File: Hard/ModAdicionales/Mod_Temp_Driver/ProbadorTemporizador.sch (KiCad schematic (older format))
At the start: 10 parts

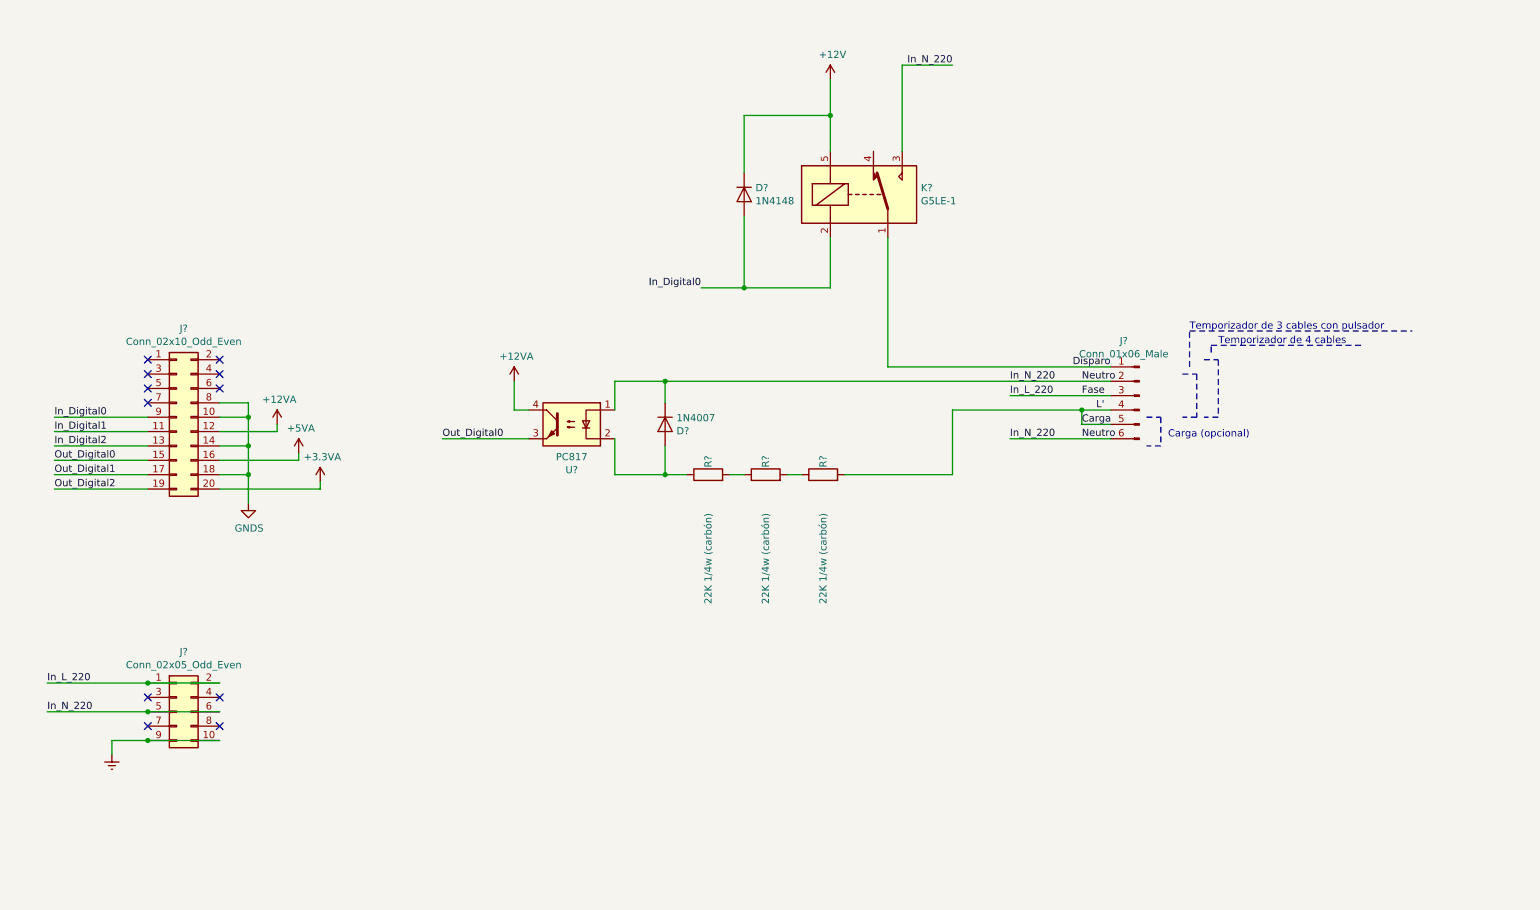
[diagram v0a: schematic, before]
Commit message: Primera correccion en modulos Adicionales y cambio de etapa de salida en modulo principal
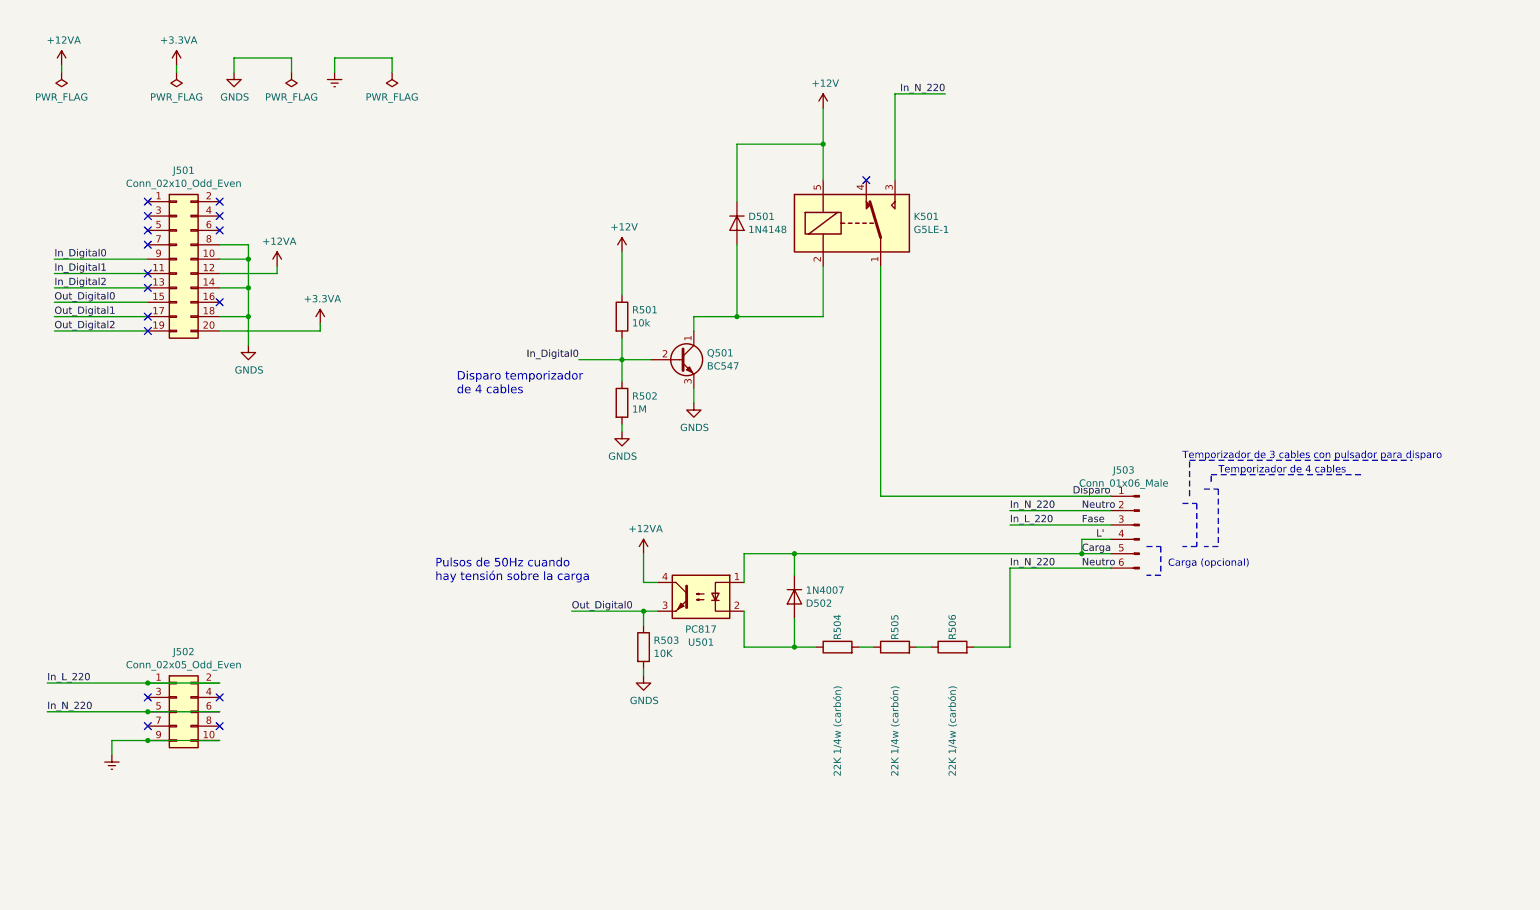
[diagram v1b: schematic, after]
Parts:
- added Q501: BC547, Package_TO_SOT_THT:TO-92_Inline, symbol Transistor_BJT:BC547
- added R501: 10k, Resistor_SMD:R_0805_2012Metric_Pad1.15x1.40mm_HandSolder, symbol Device:R
- added R502: 1M, Resistor_SMD:R_0805_2012Metric_Pad1.15x1.40mm_HandSolder, symbol Device:R
- added R503: 10K, Resistor_SMD:R_0805_2012Metric_Pad1.15x1.40mm_HandSolder, symbol Device:R
- gave numbers to parts that had none: 10
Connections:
- net +12V: now also R501.1
- net Carga: now also D502.1 (K), U501.1; no longer R506.2
- net GNDS: now also Q501.3 (E), R502.2, R503.2
- net In_Digital0: now also Q501.2 (B), R501.2, R502.1; no longer D501.2 (A), K501.2
- net In_N_220: now also R506.2; no longer D502.1 (K), U501.1
- net Out_Digital0: now also R503.1
- net +5VA: no longer names the net of J501.16 (Pin_16)
- new net: D501.2 (A), K501.2, Q501.1 (C)
- no-connect marks 11 -> 17
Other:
- note added: "Disparo temporizador\nde 4 cables"
- note added: "Pulsos de 50Hz cuando \nhay tensión sobre la carga"
- note added: "Temporizador de 3 cables con pulsador para disparo"
- note removed: "Temporizador de 3 cables con pulsador"
- moved on the sheet: D501, D502, J501, J503, K501, R504, R505, R506, U501

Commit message: Asignacion de footprints Modulos adicionales
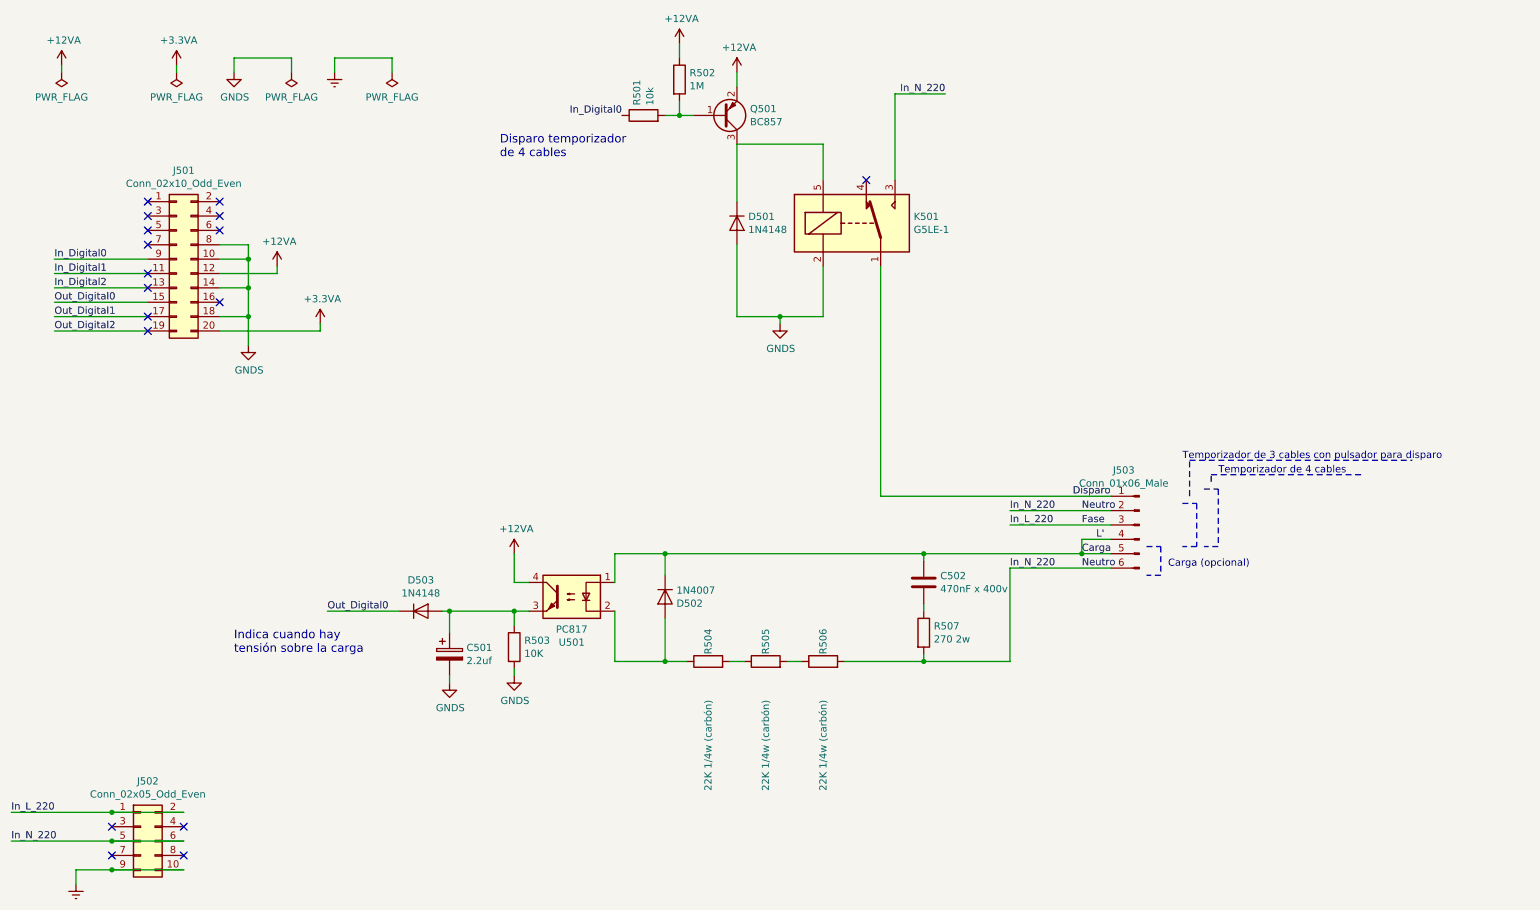
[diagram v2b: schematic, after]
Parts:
- removed Q501: BC547, Package_TO_SOT_THT:TO-92_Inline, symbol Transistor_BJT:BC547
- added C501: 2.2uf, Capacitor_THT:CP_Radial_D5.0mm_P2.00mm, symbol Device:CP
- added C502: 470nF x 400v, Capacitor_THT:C_Rect_L16.5mm_W8.7mm_P15.00mm_MKT, symbol Device:C
- added D503: 1N4148, Diode_THT:D_DO-35_SOD27_P7.62mm_Horizontal, symbol Diode:1N4148
- added Q501: BC857, Package_TO_SOT_SMD:SOT-23, symbol Transistor_BJT:BC857
- added R507: 270 2w, Resistor_THT:R_Axial_DIN0516_L15.5mm_D5.0mm_P20.32mm_Horizontal, symbol Device:R
- J501: footprint (none) -> Connector_PinHeader_2.54mm:PinHeader_2x10_P2.54mm_Horizontal
- J502: footprint (none) -> Connector_PinHeader_2.54mm:PinHeader_2x05_P2.54mm_Horizontal
- J503: footprint (none) -> TerminalBlock_Altech:Altech_AK300_1x06_P5.00mm_45-Degree
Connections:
- net +12VA: now also R502.1, Q501.2 (E)
- net Carga: now also C502.1
- net GNDS: now also D501.2 (A), K501.2, C501.2; no longer R502.2
- net In_Digital0: now also R501.1; no longer R501.2, R502.1
- net In_N_220: now also R507.2
- net Out_Digital0: now also D503.1 (K); no longer R503.1, U501.3
- net +12V: no longer names the net of D501.1 (K), K501.5
- net +12V: now also Q501.3 (C); no longer R501.1
- new net: C501.1, D503.2 (A), R503.1, U501.3
- new net: Q501.1 (B), R501.2, R502.2
- new net: C502.2, R507.1
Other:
- note added: "Indica cuando hay\ntensión sobre la carga"
- note removed: "Pulsos de 50Hz cuando \nhay tensión sobre la carga"
- moved on the sheet: D502, J502, R503, R504, R505, R506, U501

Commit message: Inicio placement de componentes en Modulos Adicionales
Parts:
- added H501, H502, H503, H504: MountingHole, MountingHole:MountingHole_3.2mm_M3, symbol Mechanical:MountingHole
- D503: footprint Diode_THT:D_DO-35_SOD27_P7.62mm_Horizontal -> Diode_SMD:D_MiniMELF
- J503: footprint TerminalBlock_Altech:Altech_AK300_1x06_P5.00mm_45-Degree -> Conectores:TerminalBlock_bornier-6_P5.00mm
- R504, R505, R506: footprint Resistor_THT:R_Axial_DIN0309_L9.0mm_D3.2mm_P12.70mm_Horizontal -> Resistor_THT:R_Axial_DIN0207_L6.3mm_D2.5mm_P7.62mm_Horizontal
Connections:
- net Carga: now also R506.2; no longer D502.1 (K), U501.1
- net In_N_220: now also D502.2 (A), U501.2; no longer R506.2
- new net: D502.1 (K), R504.1, U501.1
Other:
- moved on the sheet: R504, R505, R506
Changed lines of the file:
@@
 EESchema Schematic File Version 4
-LIBS:Mod_Temp_Driver-cache
 EELAYER 30 0
 EELAYER END
@@
 F 0 "J503" H 8958 4631 50  0000 C CNN
 F 1 "Conn_01x06_Male" H 8958 4540 50  0000 C CNN
-F 2 "TerminalBlock_Altech:Altech_AK300_1x06_P5.00mm_45-Degree" H 8850 4250 50  0001 C CNN
+F 2 "Conectores:TerminalBlock_bornier-6_P5.00mm" H 8850 4250 50  0001 C CNN
 F 3 "~" H 8850 4250 50  0001 C CNN
 	1    8850 4250
@@
 L Device:R R?
 U 1 1 5F49E33D
-P 6650 5200
+P 6650 4450
 AR Path="/5ED5374F/5F49E33D" Ref="R?"  Part="1"
 AR Path="/5ED5374F/5F0ECABF/5F49E33D" Ref="R?"  Part="1"
 AR Path="/5ED538D0/5F49E33D" Ref="R506"  Part="1"
-F 0 "R506" H 6700 5200 50  0000 L CNN
-F 1 "22K 1/4w (carbón)" H 5750 5200 50  0000 L CNN
-F 2 "Resistor_THT:R_Axial_DIN0309_L9.0mm_D3.2mm_P12.70mm_Horizontal" V 6580 5200 50  0001 C CNN
-F 3 "~" H 6650 5200 50  0001 C CNN
-	1    6650 5200
+F 0 "R506" H 6700 4450 50  0000 L CNN
+F 1 "22K 1/4w (carbón)" H 5750 4450 50  0000 L CNN
+F 2 "Resistor_THT:R_Axial_DIN0207_L6.3mm_D2.5mm_P7.62mm_Horizontal" V 6580 4450 50  0001 C CNN
+F 3 "~" H 6650 4450 50  0001 C CNN
+	1    6650 4450
 	0    -1   -1   0
 $EndComp
@@
 L Device:R R?
 U 1 1 5F49E343
-P 6250 5200
+P 6250 4450
 AR Path="/5ED5374F/5F49E343" Ref="R?"  Part="1"
 AR Path="/5ED5374F/5F0ECABF/5F49E343" Ref="R?"  Part="1"
 AR Path="/5ED538D0/5F49E343" Ref="R505"  Part="1"
-F 0 "R505" H 6300 5200 50  0000 L CNN
-F 1 "22K 1/4w (carbón)" H 5350 5200 50  0000 L CNN
-F 2 "Resistor_THT:R_Axial_DIN0309_L9.0mm_D3.2mm_P12.70mm_Horizontal" V 6180 5200 50  0001 C CNN
-F 3 "~" H 6250 5200 50  0001 C CNN
-	1    6250 5200
+F 0 "R505" H 6300 4450 50  0000 L CNN
+F 1 "22K 1/4w (carbón)" H 5350 4450 50  0000 L CNN
+F 2 "Resistor_THT:R_Axial_DIN0207_L6.3mm_D2.5mm_P7.62mm_Horizontal" V 6180 4450 50  0001 C CNN
+F 3 "~" H 6250 4450 50  0001 C CNN
+	1    6250 4450
 	0    -1   -1   0
 $EndComp
@@
 L Device:R R?
 U 1 1 5F49E349
-P 5850 5200
+P 5850 4450
 AR Path="/5ED5374F/5F49E349" Ref="R?"  Part="1"
 AR Path="/5ED5374F/5F0ECABF/5F49E349" Ref="R?"  Part="1"
 AR Path="/5ED538D0/5F49E349" Ref="R504"  Part="1"
-F 0 "R504" H 5900 5200 50  0000 L CNN
-F 1 "22K 1/4w (carbón)" H 4950 5200 50  0000 L CNN
-F 2 "Resistor_THT:R_Axial_DIN0309_L9.0mm_D3.2mm_P12.70mm_Horizontal" V 5780 5200 50  0001 C CNN
-F 3 "~" H 5850 5200 50  0001 C CNN
-	1    5850 5200
+F 0 "R504" H 5900 4450 50  0000 L CNN
+F 1 "22K 1/4w (carbón)" H 4950 4450 50  0000 L CNN
+F 2 "Resistor_THT:R_Axial_DIN0207_L6.3mm_D2.5mm_P7.62mm_Horizontal" V 5780 4450 50  0001 C CNN
+F 3 "~" H 5850 4450 50  0001 C CNN
+	1    5850 4450
 	0    -1   -1   0
 $EndComp
 Wire Wire Line
-	6000 5200 6100 5200
-Wire Wire Line
-	6400 5200 6500 5200
+	6000 4450 6100 4450
+Wire Wire Line
+	6400 4450 6500 4450
 Wire Wire Line
 	8650 4350 8450 4350
@@
 	8650 4150 7950 4150
 Wire Wire Line
-	5550 4450 7350 4450
-Connection ~ 5550 4450
+	5550 5200 7350 5200
 Wire Wire Line
 	8650 4550 7950 4550
@@
 F 0 "D503" H 3850 5066 50  0000 C CNN
 F 1 "1N4148" H 3850 4975 50  0000 C CNN
-F 2 "Diode_THT:D_DO-35_SOD27_P7.62mm_Horizontal" H 3850 4675 50  0001 C CNN
+F 2 "Diode_SMD:D_MiniMELF" H 3850 4675 50  0001 C CNN
 F 3 "https://assets.nexperia.com/documents/data-sheet/1N4148_1N4448.pdf" H 3850 4850 50  0001 C CNN
 	1    3850 4850
@@
 Wire Wire Line
 	7350 4500 7350 4450
-Connection ~ 7350 4450
 Wire Wire Line
 	7350 4450 8450 4450
@@
 	5200 4850 5200 5200
 Wire Wire Line
-	6800 5200 7350 5200
+	6800 4450 7350 4450
+Wire Wire Line
+	5550 4900 5550 5200
+Wire Wire Line
+	5550 4450 5700 4450
+$Comp
+L Mechanical:MountingHole H?
+U 1 1 5ED84BD0
+P 9300 1150
+AR Path="/5ED5374F/5ED84BD0" Ref="H?"  Part="1"
+AR Path="/5ED538D0/5ED84BD0" Ref="H501"  Part="1"
+F 0 "H501" H 9400 1196 50  0000 L CNN
+F 1 "MountingHole" H 9400 1105 50  0000 L CNN
+F 2 "MountingHole:MountingHole_3.2mm_M3" H 9300 1150 50  0001 C CNN
+F 3 "~" H 9300 1150 50  0001 C CNN
+	1    9300 1150
+	1    0    0    -1
+$EndComp
+$Comp
+L Mechanical:MountingHole H?
+U 1 1 5ED84BD6
+P 10300 1150
+AR Path="/5ED5374F/5ED84BD6" Ref="H?"  Part="1"
+AR Path="/5ED538D0/5ED84BD6" Ref="H503"  Part="1"
+F 0 "H503" H 10400 1196 50  0000 L CNN
+F 1 "MountingHole" H 10400 1105 50  0000 L CNN
+F 2 "MountingHole:MountingHole_3.2mm_M3" H 10300 1150 50  0001 C CNN
+F 3 "~" H 10300 1150 50  0001 C CNN
+	1    10300 1150
+	1    0    0    -1
+$EndComp
+$Comp
+L Mechanical:MountingHole H?
+U 1 1 5ED84BDC
+P 9300 1550
+AR Path="/5ED5374F/5ED84BDC" Ref="H?"  Part="1"
+AR Path="/5ED538D0/5ED84BDC" Ref="H502"  Part="1"
+F 0 "H502" H 9400 1596 50  0000 L CNN
+F 1 "MountingHole" H 9400 1505 50  0000 L CNN
+F 2 "MountingHole:MountingHole_3.2mm_M3" H 9300 1550 50  0001 C CNN
+F 3 "~" H 9300 1550 50  0001 C CNN
+	1    9300 1550
+	1    0    0    -1
+$EndComp
+$Comp
+L Mechanical:MountingHole H?
+U 1 1 5ED84BE2
+P 10300 1550
+AR Path="/5ED5374F/5ED84BE2" Ref="H?"  Part="1"
+AR Path="/5ED538D0/5ED84BE2" Ref="H504"  Part="1"
+F 0 "H504" H 10400 1596 50  0000 L CNN
+F 1 "MountingHole" H 10400 1505 50  0000 L CNN
+F 2 "MountingHole:MountingHole_3.2mm_M3" H 10300 1550 50  0001 C CNN
+F 3 "~" H 10300 1550 50  0001 C CNN
+	1    10300 1550
+	1    0    0    -1
+$EndComp
+Connection ~ 7350 4450
+Connection ~ 5550 4450
+Connection ~ 5550 5200
 Connection ~ 7350 5200
-Wire Wire Line
-	5550 4900 5550 5200
-Connection ~ 5550 5200
-Wire Wire Line
-	5550 5200 5700 5200
 $EndSCHEMATC

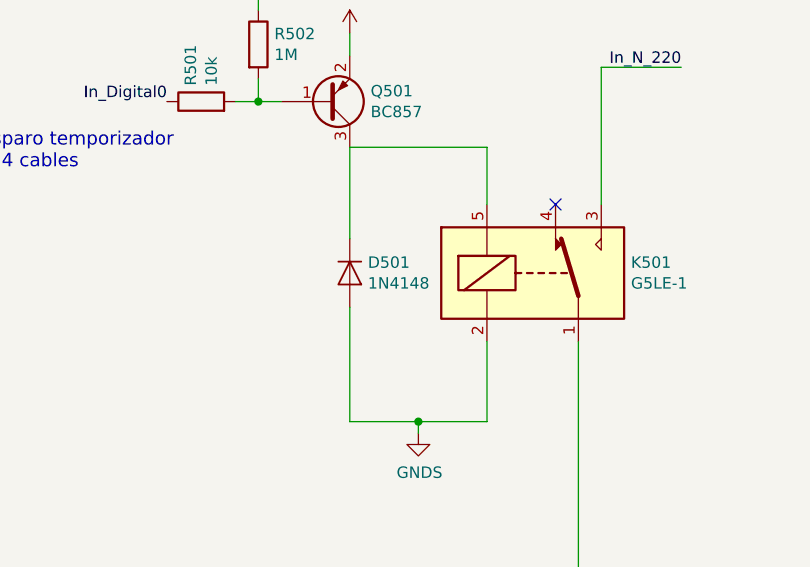
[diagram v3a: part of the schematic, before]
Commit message: Avance en trazado de pistas Modulos Adicionales
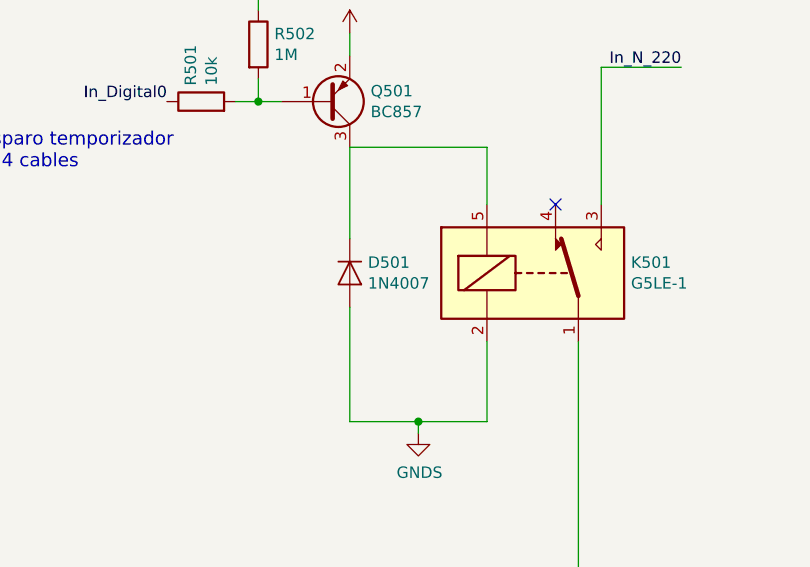
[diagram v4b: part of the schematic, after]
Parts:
- removed D501: 1N4148, Diode_THT:D_DO-35_SOD27_P7.62mm_Horizontal, symbol Diode:1N4148
- added D501: 1N4007, Diode_THT:D_DO-41_SOD81_P10.16mm_Horizontal, symbol Diode:1N4007
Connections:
- net GNDS: now also D501.2 (A)
- net at K501.5, Q501.3 (C): now also D501.1 (K)
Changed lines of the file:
@@
 	1    0    0    -1
-$EndComp
-$Comp
-L Diode:1N4148 D?
-U 1 1 5F40154B
-P 6050 2150
-AR Path="/5ED5374F/5F20E931/5F40154B" Ref="D?"  Part="1"
-AR Path="/5ED538D0/5F40154B" Ref="D501"  Part="1"
-F 0 "D501" V 6004 2229 50  0000 L CNN
-F 1 "1N4148" V 6095 2229 50  0000 L CNN
-F 2 "Diode_THT:D_DO-35_SOD27_P7.62mm_Horizontal" H 6050 1975 50  0001 C CNN
-F 3 "https://assets.nexperia.com/documents/data-sheet/1N4148_1N4448.pdf" H 6050 2150 50  0001 C CNN
-	1    6050 2150
-	0    1    1    0
 $EndComp
 Wire Wire Line
@@
 Connection ~ 5550 5200
 Connection ~ 7350 5200
+$Comp
+L Diode:1N4007 D?
+U 1 1 5EEDCA26
+P 6050 2150
+AR Path="/5ED5374F/5F20E931/5EEDCA26" Ref="D?"  Part="1"
+AR Path="/5ED538D0/5EEDCA26" Ref="D501"  Part="1"
+F 0 "D501" V 6004 2229 50  0000 L CNN
+F 1 "1N4007" V 6095 2229 50  0000 L CNN
+F 2 "Diode_THT:D_DO-41_SOD81_P10.16mm_Horizontal" H 6050 1975 50  0001 C CNN
+F 3 "http://www.vishay.com/docs/88503/1n4001.pdf" H 6050 2150 50  0001 C CNN
+	1    6050 2150
+	0    1    1    0
+$EndComp
 $EndSCHEMATC
